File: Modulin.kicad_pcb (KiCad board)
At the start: 2 copper layers, 63.5 x 108.6 mm, 84 parts, among them J1 Conn_01x03_Male, J10 Conn_01x10_Male, J11 DIN-5_180degree, J12 Audio-Jack-2, J2 Conn_01x03_Male, J3 Conn_01x03_Female, J4 Conn_01x03_Female, J5 Conn_01x02_Male, J6 Conn_01x10_Male, J7 Conn_01x10_Male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

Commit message: Finished board Rev 1
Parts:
- moved R10 0.30 mm to (127.5, 133.1)
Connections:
- C25 pad 1: GNDA -> GNDD
- C26 pad 2: GNDA -> GNDD
- C5 pad 2: GNDA -> GNDD
- C6 pad 2: GNDA -> GNDD
- J12 pad 2: GNDA -> GNDD
- R22 pad 2: GNDA -> GNDD
- U3 pad 9: GNDA -> GNDD
- U9 pad 4: GNDA -> GNDD
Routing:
- net GNDD: track 121.2 -> 337.1 mm, vias 2 -> 23
- net DVCC: track 137.2 -> 301.4 mm, vias 4 -> 19
- net /FR2311_setup1/P2.3: track 7.87 -> 99.4 mm, vias 0 -> 6
- net /RGB_Encoder/A: track 29.4 -> 108.4 mm, vias 0 -> 1
- net /FR2311_setup2/P1.6: track 31.2 -> 102.9 mm, vias 0 -> 3
- net /RGB_Encoder/B: track 30.2 -> 93.0 mm, vias 0 -> 3
- net +5V: track 5.26 -> 66.4 mm, vias 0 -> 3
- net /FR2311_setup2/P2.0: track 32.8 -> 89.8 mm, vias 0 -> 3
- net +9V: track 24.0 -> 77.3 mm, vias 0 -> 4
- net /FR2311_setup2/P2.1: track 33.5 -> 77.9 mm, vias 0 -> 2
- net GNDA: track 35.9 -> 0.00 mm
- net Net-(U4-Pad4): track 0.00 -> 34.8 mm, vias 0 -> 4
- net /FR2311_setup1/P2.4: track 78.6 -> 105.1 mm, vias 3 -> 6
- net /RGB_Encoder/Btn: track 33.9 -> 57.5 mm, vias 0 -> 1
- net /FR2311_setup2/P1.0: track 27.2 -> 45.9 mm, vias 0 -> 2
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- added copper zone on B.Cu, net GNDD
- added copper zone on F.Cu, net GNDD
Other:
- board text added: ""Modulin" for Intro to Embedded Systems"
- board text added: "3.3V"
- board text added: "9V"
- board text added: "DVCC"
- board text added: "Ext"
- board text added: "GND"
- board text added: "Int"
- board text added: "Lonnie L. Souder II"
- board text added: "Supply"

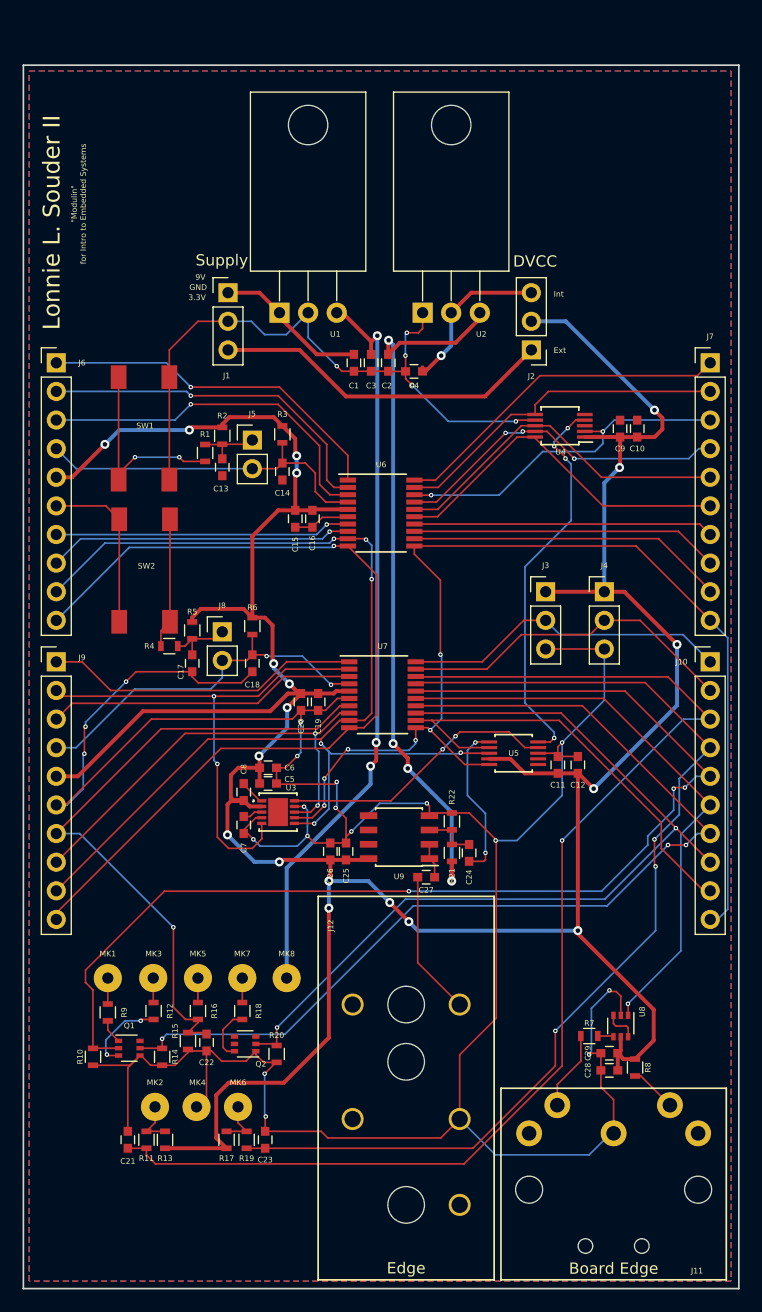
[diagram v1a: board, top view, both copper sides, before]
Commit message: Tested basic functions of SPILib
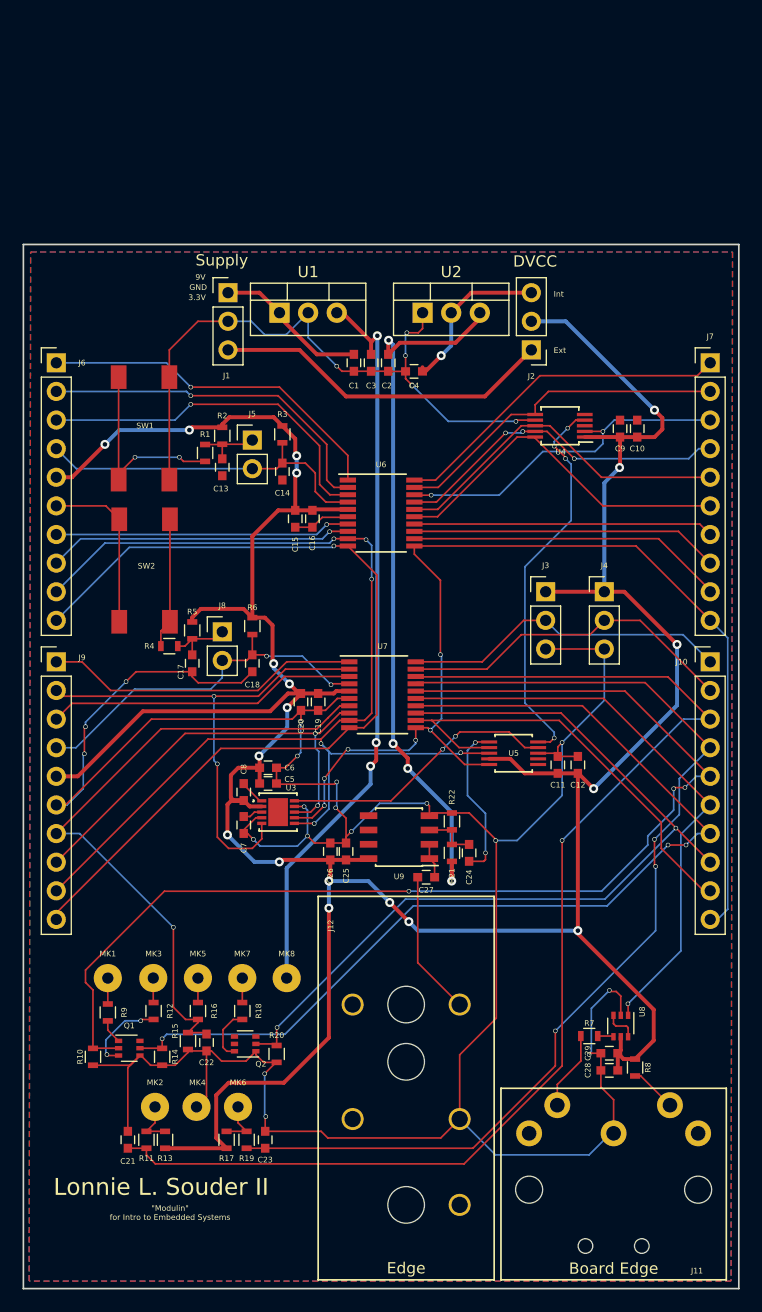
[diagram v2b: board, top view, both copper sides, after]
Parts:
- U1, U2: footprint TO_SOT_Packages_THT:TO-220-3_Horizontal -> TO_SOT_Packages_THT:TO-220-3_Vertical
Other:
- board size 63.5 x 108.6 mm -> 63.5 x 92.7 mm
- net class Small: via_drill 0.2 -> 0.3
